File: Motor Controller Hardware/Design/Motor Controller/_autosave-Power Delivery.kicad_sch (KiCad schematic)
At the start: 38 parts, among them J16 Supply Input, Q3 NMOS, Q4 NMOS, Q5 NMOS, SW2 Power Stage Enable Override, SW3 Motor Controller Enable Overr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, U15 LM74700, U16 TPS26631RGE

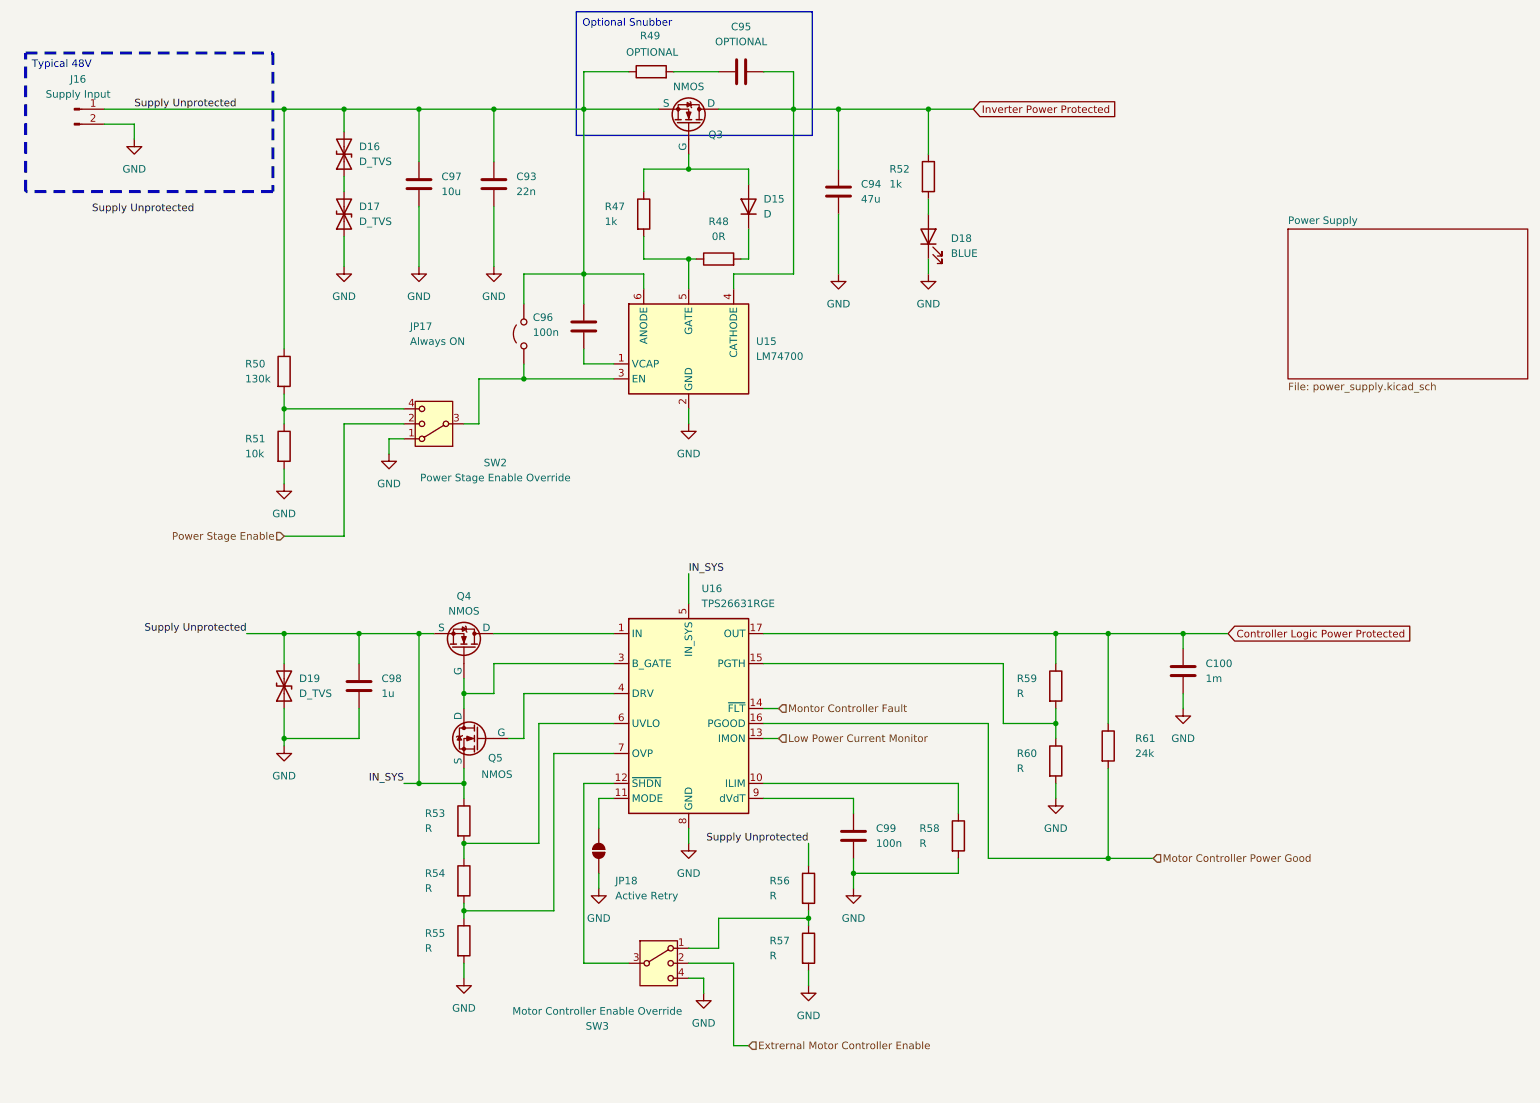
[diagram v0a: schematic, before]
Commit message: Started power delivery
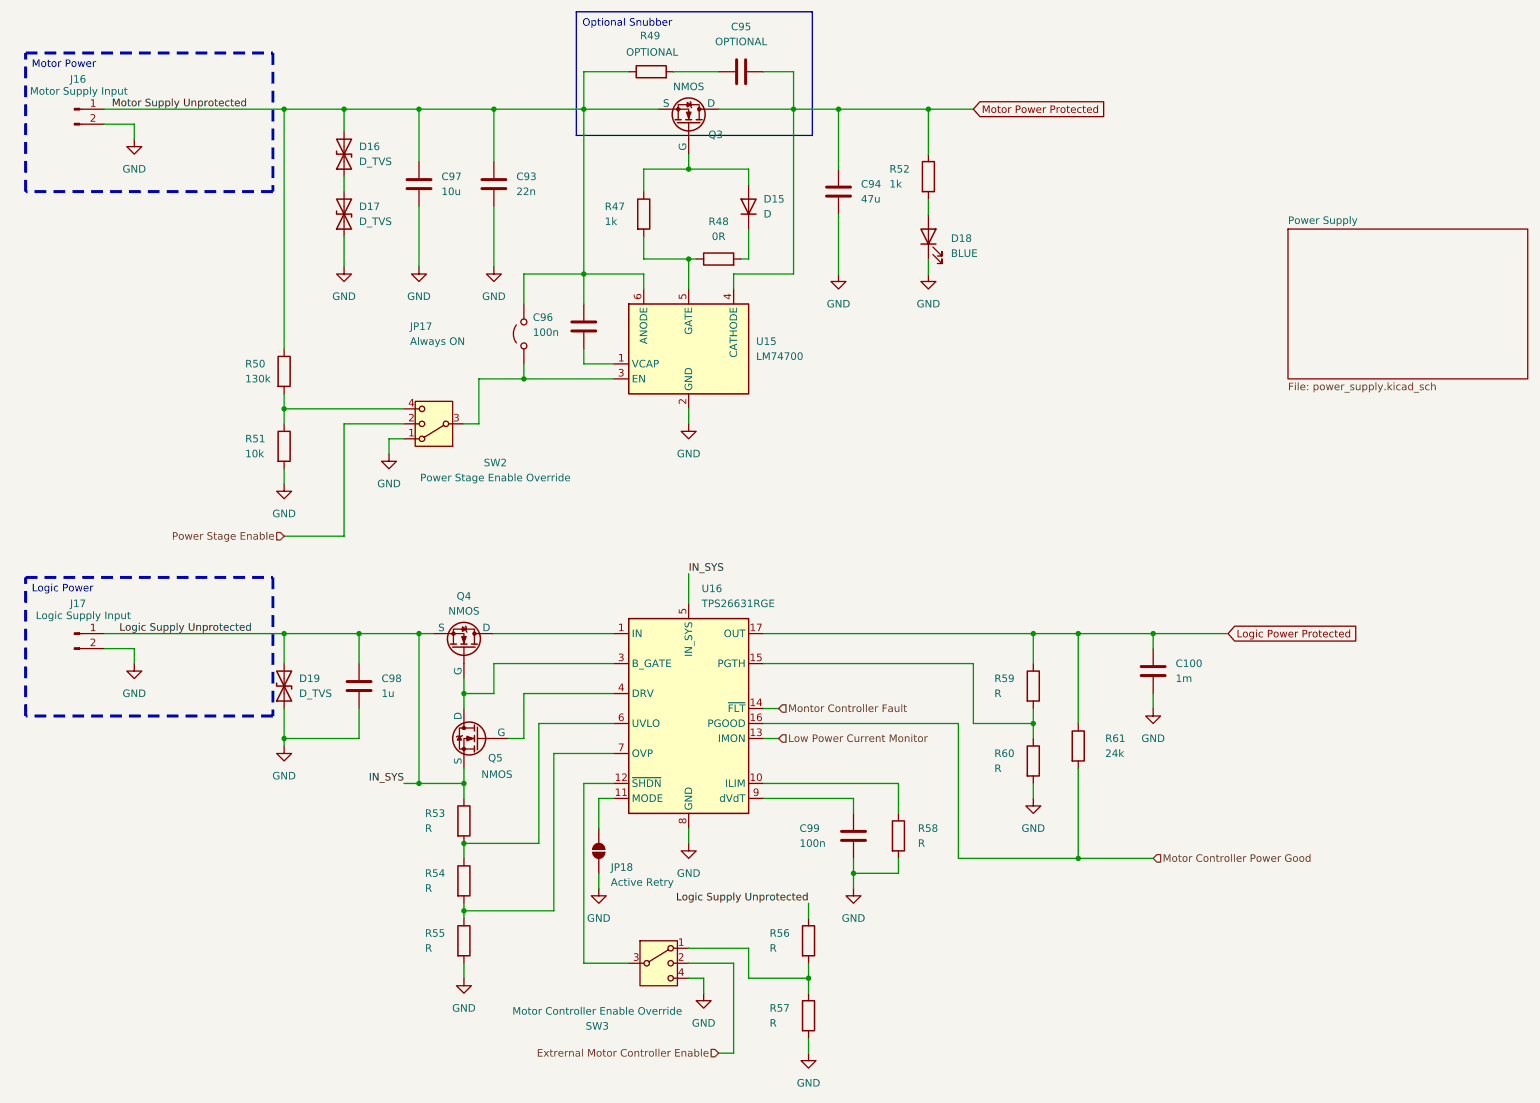
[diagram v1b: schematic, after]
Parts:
- added J17: Logic Supply Input, symbol Connector:Conn_01x02_Pin
- J16: value Supply Input -> Motor Supply Input
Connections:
- net GND: now also J17.2 (Pin_2)
- net IN_SYS: now also J17.1 (Pin_1); no longer C93.1, C96.2, C97.1, D16.2 (A2), J16.1 (Pin_1), JP17.2 (B), Q3.3 (S), R49.1, R50.1, U15.6 (ANODE)
- net Controller Logic Power Protected renamed Logic Power Protected
- net Inverter Power Protected renamed Motor Power Protected
- new net Motor Supply Unprotected: C93.1, C96.2, C97.1, D16.2 (A2), J16.1 (Pin_1), JP17.2 (B), Q3.3 (S), R49.1, R50.1, U15.6 (ANODE)
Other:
- moved on the sheet: C100, R56, R57, R58, R59, R60, R61
